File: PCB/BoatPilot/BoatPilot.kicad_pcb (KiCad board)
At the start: 2 copper layers, 40 x 40 mm, 87 parts, among them J101 battery, J102 switch, J103 SWD, J104 wind, J105 RC, J106 GPS, J108 failsafe, J109 SERVO1, J110 SERVO2, J111 SERVO3, J201 GPIO, J202 USB-Audio-IR, J203 Audio-UART, P101 ICT-Point, P102 ICT-Point, P103 ICT-Point, P104 ICT-Point, P105 ICT-Point, P106 ICT-Point, P107 ICT-Point, P108 ICT-Point, P109 ICT-Point, P113 ICT-Point, P119 ICT-Point, P129 ICT-Point, P130 ICT-Point, P132 ICT-Point, P133 ICT-Point, P134 ICT-Point, P135 ICT-Point, Q101 TSM3457, U101 GY-91, U102 74LVC1G97, U103 LM1117-3.3, U104 TPS565208, U105 24LC512, U106 74LVC1G97, U108 74LVC1G97, U109 STM32F103C8Tx, Y101 8MHz

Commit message: Add DMC to project
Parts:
- added Barcode**: BoatPilot, footprint:BoatPilot, B.Cu at (139.2, 106.6)
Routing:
- net +BATT: track 53.1 -> 55.0 mm
- net +5V: track 115.5 -> 117.0 mm
- net GND: vias 75 -> 69

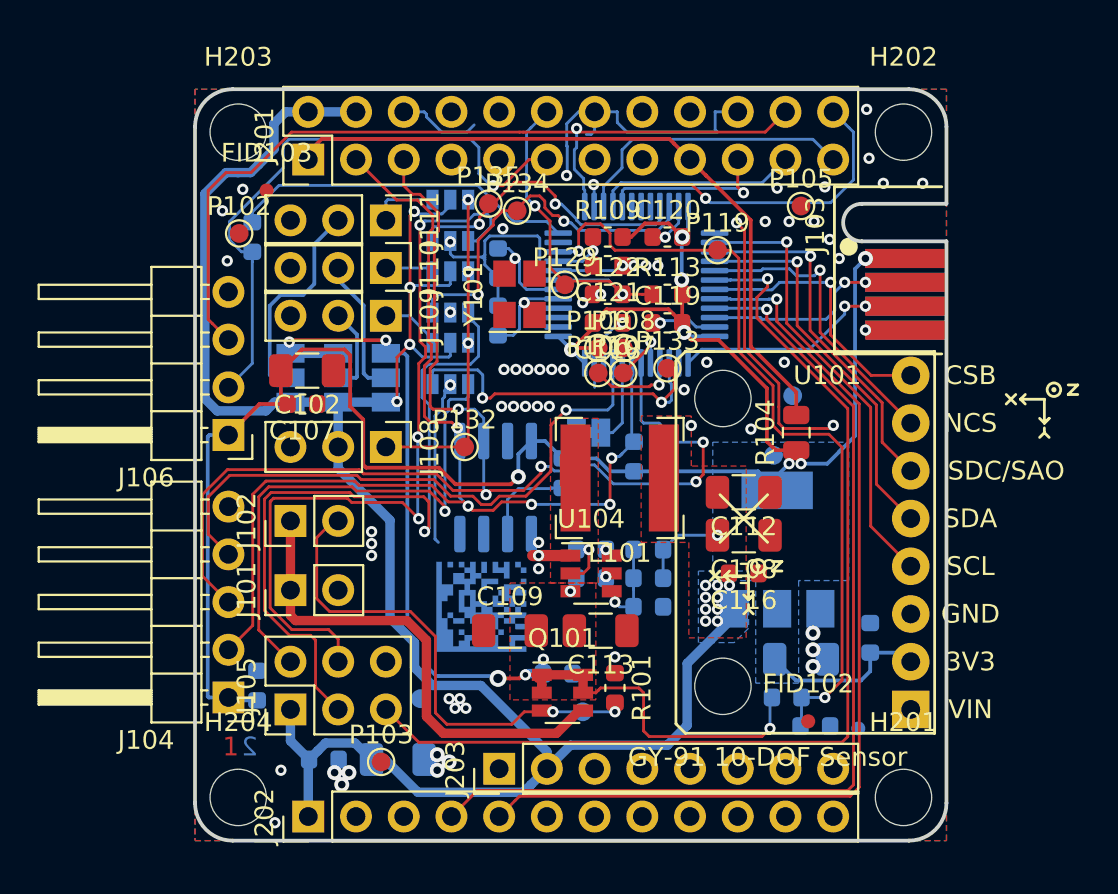
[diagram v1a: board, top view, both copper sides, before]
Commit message: Update layout
Change the LM1117 to a smaller sized LDO and adapt the layout.
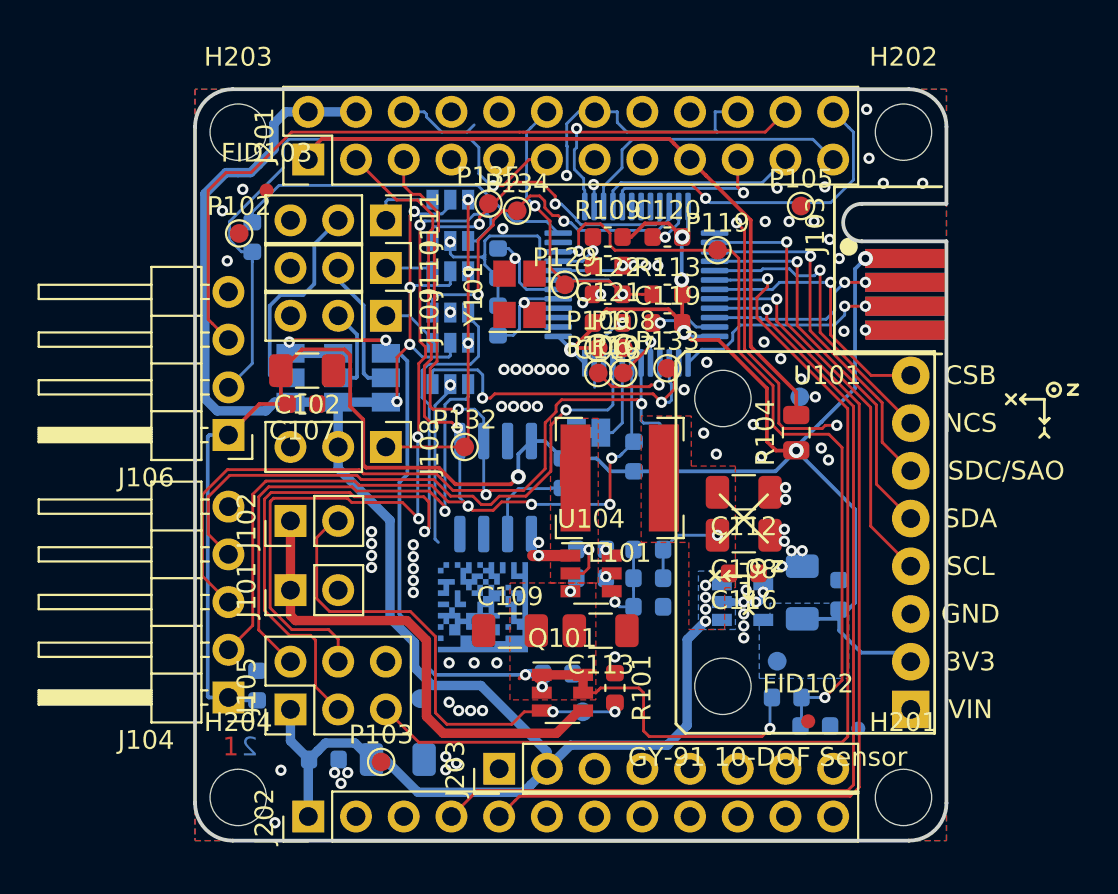
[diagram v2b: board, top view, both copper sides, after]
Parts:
- U103: value LM1117-3.3 -> TLV75733PDBV; footprint Package_TO_SOT_SMD:SOT-223-3_TabPin2 -> Package_TO_SOT_SMD:SOT-23-5
- moved P130 11.0 mm to (155.0, 109.4)
- moved C111 3.56 mm to (156.3, 105.8), turned to 270 degrees
- moved U103 3.35 mm to (153.1, 106.3), turned to 0 degrees
- moved C103 2.82 mm to (158.3, 105.9)
- moved P104 0.39 mm to (156.2, 95.4)
- moved Barcode** 0.09 mm to (139.3, 106.6), turned to 180 degrees
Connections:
- J201 pad 10: /FriednlyARM NanoPi Air/RX1 -> (no net)
- J201 pad 13: /FriednlyARM NanoPi Air/RTS2_PA2 -> (no net)
- J201 pad 15: /FriednlyARM NanoPi Air/CTS2_PA3 -> (no net)
- J201 pad 16: /FriednlyARM NanoPi Air/RTS1 -> (no net)
- J201 pad 18: /FriednlyARM NanoPi Air/CTS1 -> (no net)
- J201 pad 7: /FriednlyARM NanoPi Air/PG11 -> (no net)
- J201 pad 8: /FriednlyARM NanoPi Air/TX1 -> (no net)
- J202 pad 10: /FriednlyARM NanoPi Air/I2S_DOUT -> (no net)
- J202 pad 11: /FriednlyARM NanoPi Air/I2S_DIN -> (no net)
- J202 pad 2: /FriednlyARM NanoPi Air/D1P -> (no net)
- J202 pad 3: /FriednlyARM NanoPi Air/D1N -> (no net)
- J202 pad 6: /FriednlyARM NanoPi Air/PL11_IR -> (no net)
- J202 pad 7: /FriednlyARM NanoPi Air/PA17_SPDIF -> (no net)
- J202 pad 8: /FriednlyARM NanoPi Air/I2S_LRCK -> (no net)
- J202 pad 9: /FriednlyARM NanoPi Air/I2S_BCK -> (no net)
- J203 pad 3: /FriednlyARM NanoPi Air/TX0 -> (no net)
- J203 pad 4: /FriednlyARM NanoPi Air/RX0 -> (no net)
- J203 pad 5: /FriednlyARM NanoPi Air/LL -> (no net)
- J203 pad 6: /FriednlyARM NanoPi Air/LR -> (no net)
- J203 pad 7: /FriednlyARM NanoPi Air/MN -> (no net)
- J203 pad 8: /FriednlyARM NanoPi Air/MP -> (no net)
- U101 pad 1: Net-(U101-Pad1) -> (no net)
- U103 pad 1: GND -> +5V
- U103 pad 2: +3V3 -> GND
- U109 pad 11: Net-(U109-Pad11) -> (no net)
- U109 pad 18: Net-(U109-Pad18) -> (no net)
- U109 pad 19: Net-(U109-Pad19) -> (no net)
- U109 pad 2: Net-(U109-Pad2) -> (no net)
- U109 pad 20: Net-(U109-Pad20) -> (no net)
- U109 pad 25: Net-(U109-Pad25) -> (no net)
- U109 pad 3: Net-(U109-Pad3) -> (no net)
- U109 pad 38: Net-(U109-Pad38) -> (no net)
- U109 pad 4: Net-(U109-Pad4) -> (no net)
- U109 pad 46: Net-(U109-Pad46) -> (no net)
- Y101 pad 2: Net-(Y101-Pad2) -> (no net)
- Y101 pad 4: Net-(Y101-Pad4) -> (no net)
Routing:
- net +3V3: track 121.4 -> 128.1 mm, vias 8 -> 7
- net /I2C1_SCL: track 66.5 -> 61.5 mm, vias 5 -> 3
- net GND: track 79.6 -> 81.1 mm, vias 69 -> 95
- net +5V: track 117.0 -> 116.4 mm, vias 14 -> 9
- net +BATT: track 55.0 -> 55.2 mm, vias 7 -> 6

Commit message: Add USB pull-up resistor and connector
Add the missing pull-up resistors to the USB line and add a mini-usb
header to the board
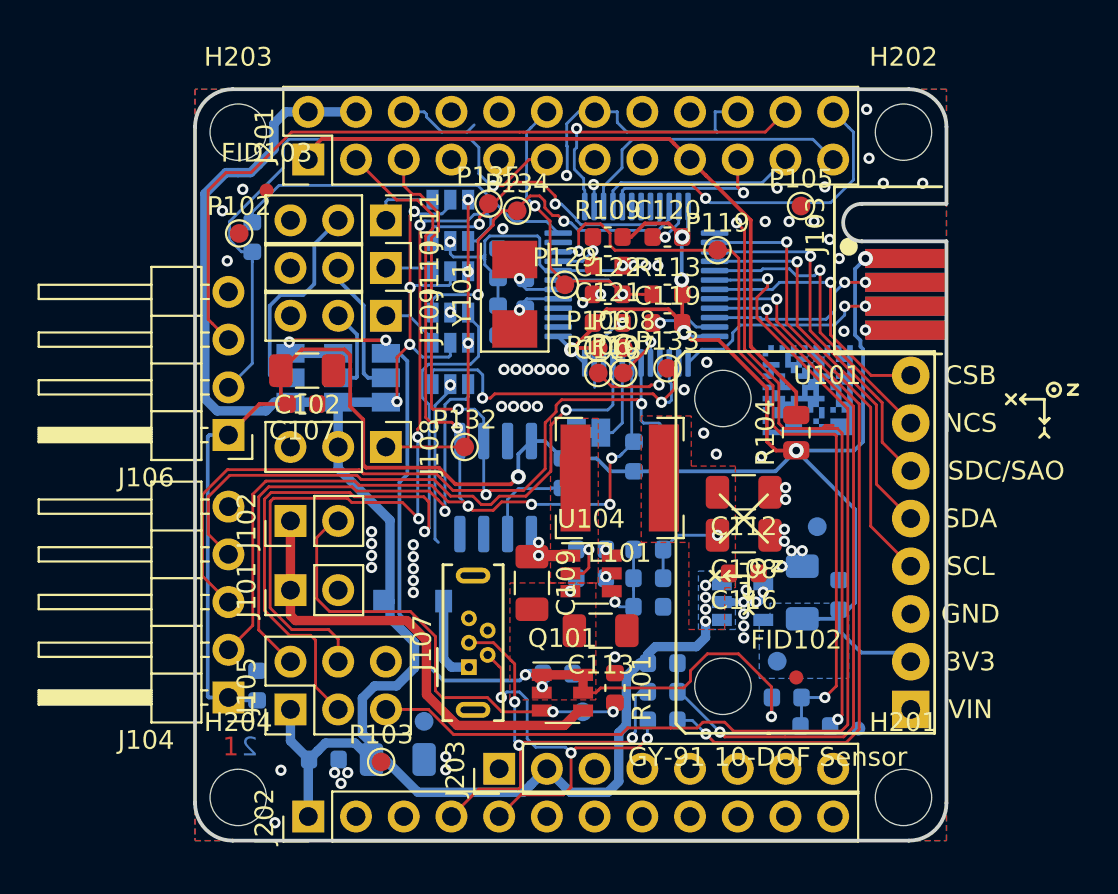
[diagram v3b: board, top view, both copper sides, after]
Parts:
- added D101: 1N4417, Diode_SMD:D_SOD-123, B.Cu at (135.6, 106.2)
- added J107: USB_OTG, Connector_USB:USB_Micro-B_Wuerth_614105150721_Vertical, F.Cu at (138.6, 109.8)
- added R107: 20R, Resistor_SMD:R_0603_1608Metric, B.Cu at (148.9, 111.1)
- added R108: 20R, Resistor_SMD:R_0603_1608Metric, B.Cu at (148.9, 112.6)
- added R112: 4.64k, Resistor_SMD:R_0603_1608Metric, B.Cu at (148.9, 109.6)
- added R116: 1M, Resistor_SMD:R_0603_1608Metric, B.Cu at (141.6, 89.9)
- Y101: footprint Crystal:Crystal_SMD_SeikoEpson_FA238-4Pin_3.2x2.5mm -> Crystal:Crystal_SMD_5032-2Pin_5.0x3.2mm
- moved Barcode** 20.8 mm to (156.6, 95.0)
- moved P104 6.97 mm to (157.1, 102.3)
- moved C109 2.80 mm to (141.9, 105.3), turned to 270 degrees
- moved FID102 2.42 mm to (156.0, 110.3)
- moved P101 1.22 mm to (136.2, 112.7)
- moved Y101 0.25 mm to (141.0, 89.9)
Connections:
- J201 pad 10: (no net) -> /FriednlyARM NanoPi Air/RX1
- J201 pad 13: (no net) -> /FriednlyARM NanoPi Air/RTS2_PA2
- J201 pad 15: (no net) -> /FriednlyARM NanoPi Air/CTS2_PA3
- J201 pad 16: (no net) -> /FriednlyARM NanoPi Air/RTS1
- J201 pad 18: (no net) -> /FriednlyARM NanoPi Air/CTS1
- J201 pad 7: (no net) -> /FriednlyARM NanoPi Air/PG11
- J201 pad 8: (no net) -> /FriednlyARM NanoPi Air/TX1
- J202 pad 10: (no net) -> /FriednlyARM NanoPi Air/I2S_DOUT
- J202 pad 11: (no net) -> /FriednlyARM NanoPi Air/I2S_DIN
- J202 pad 2: (no net) -> /FriednlyARM NanoPi Air/D1P
- J202 pad 3: (no net) -> /FriednlyARM NanoPi Air/D1N
- J202 pad 6: (no net) -> /FriednlyARM NanoPi Air/PL11_IR
- J202 pad 7: (no net) -> /FriednlyARM NanoPi Air/PA17_SPDIF
- J202 pad 8: (no net) -> /FriednlyARM NanoPi Air/I2S_LRCK
- J202 pad 9: (no net) -> /FriednlyARM NanoPi Air/I2S_BCK
- J203 pad 3: (no net) -> /FriednlyARM NanoPi Air/TX0
- J203 pad 4: (no net) -> /FriednlyARM NanoPi Air/RX0
- J203 pad 5: (no net) -> /FriednlyARM NanoPi Air/LL
- J203 pad 6: (no net) -> /FriednlyARM NanoPi Air/LR
- J203 pad 7: (no net) -> /FriednlyARM NanoPi Air/MN
- J203 pad 8: (no net) -> /FriednlyARM NanoPi Air/MP
- U101 pad 1: (no net) -> Net-(U101-Pad1)
- U109 pad 11: (no net) -> Net-(U109-Pad11)
- U109 pad 18: (no net) -> Net-(U109-Pad18)
- U109 pad 19: (no net) -> Net-(U109-Pad19)
- U109 pad 2: (no net) -> Net-(U109-Pad2)
- U109 pad 20: (no net) -> Net-(U109-Pad20)
- U109 pad 25: (no net) -> Net-(U109-Pad25)
- U109 pad 3: (no net) -> Net-(U109-Pad3)
- U109 pad 32: /USBD- -> /PA11
- U109 pad 33: /USBD+ -> /PA12
- U109 pad 38: (no net) -> Net-(U109-Pad38)
- U109 pad 4: (no net) -> Net-(U109-Pad4)
- U109 pad 46: (no net) -> Net-(U109-Pad46)
- Y101 pad 2: (no net) -> Net-(C124-Pad2)
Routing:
- net /PA12: track 0.00 -> 39.2 mm, vias 0 -> 2
- net /PA11: track 0.00 -> 38.5 mm, vias 0 -> 2
- net /USBD-: track 50.9 -> 20.6 mm, vias 1 -> 3
- net /USBD+: track 52.1 -> 23.2 mm, vias 1 -> 3
- net GND: track 81.1 -> 97.6 mm, vias 95 -> 80
- net Net-(D101-Pad2): track 0.00 -> 4.61 mm
- net +3V3: track 128.1 -> 130.5 mm
- net Net-(J102-Pad2): track 26.7 -> 25.4 mm
- net Net-(J101-Pad1): track 26.3 -> 25.3 mm
- net Net-(C124-Pad2): track 5.86 -> 6.87 mm

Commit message: Fix DRC errors and optimise USB lines
Fix the DRC errors and remove the strip lines from the USB data lines.
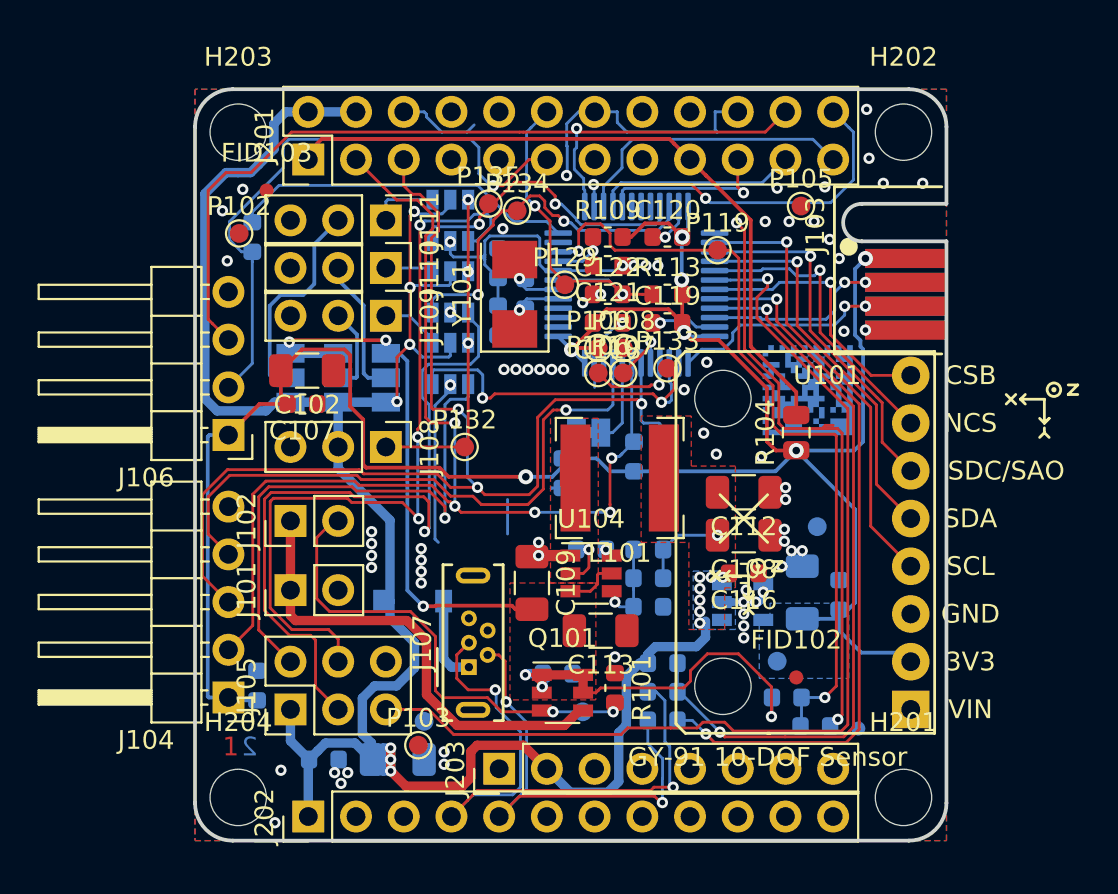
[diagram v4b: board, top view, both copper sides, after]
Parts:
- removed R106: 10k, Resistor_SMD:R_0603_1608Metric
- removed U105: 24LC512, Package_SO:SOIC-8_3.9x4.9mm_P1.27mm
- moved P103 2.17 mm to (135.9, 113.9)
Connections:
- J107 pad 4: Net-(J107-Pad4) -> (no net)
- J201 pad 10: /FriednlyARM NanoPi Air/RX1 -> (no net)
- J201 pad 13: /FriednlyARM NanoPi Air/RTS2_PA2 -> (no net)
- J201 pad 15: /FriednlyARM NanoPi Air/CTS2_PA3 -> (no net)
- J201 pad 16: /FriednlyARM NanoPi Air/RTS1 -> (no net)
- J201 pad 18: /FriednlyARM NanoPi Air/CTS1 -> (no net)
- J201 pad 7: /FriednlyARM NanoPi Air/PG11 -> (no net)
- J201 pad 8: /FriednlyARM NanoPi Air/TX1 -> (no net)
- J202 pad 10: /FriednlyARM NanoPi Air/I2S_DOUT -> (no net)
- J202 pad 11: /FriednlyARM NanoPi Air/I2S_DIN -> (no net)
- J202 pad 2: /FriednlyARM NanoPi Air/D1P -> (no net)
- J202 pad 3: /FriednlyARM NanoPi Air/D1N -> (no net)
- J202 pad 6: /FriednlyARM NanoPi Air/PL11_IR -> (no net)
- J202 pad 7: /FriednlyARM NanoPi Air/PA17_SPDIF -> (no net)
- J202 pad 8: /FriednlyARM NanoPi Air/I2S_LRCK -> (no net)
- J202 pad 9: /FriednlyARM NanoPi Air/I2S_BCK -> (no net)
- J203 pad 3: /FriednlyARM NanoPi Air/TX0 -> (no net)
- J203 pad 4: /FriednlyARM NanoPi Air/RX0 -> (no net)
- J203 pad 5: /FriednlyARM NanoPi Air/LL -> (no net)
- J203 pad 6: /FriednlyARM NanoPi Air/LR -> (no net)
- J203 pad 7: /FriednlyARM NanoPi Air/MN -> (no net)
- J203 pad 8: /FriednlyARM NanoPi Air/MP -> (no net)
- U101 pad 1: Net-(U101-Pad1) -> (no net)
- U104 pad 5: Net-(R106-Pad1) -> +BATT
- U109 pad 11: Net-(U109-Pad11) -> (no net)
- U109 pad 18: Net-(U109-Pad18) -> (no net)
- U109 pad 19: Net-(U109-Pad19) -> (no net)
- U109 pad 2: Net-(U109-Pad2) -> (no net)
- U109 pad 20: Net-(U109-Pad20) -> (no net)
- U109 pad 25: Net-(U109-Pad25) -> (no net)
- U109 pad 3: Net-(U109-Pad3) -> (no net)
- U109 pad 38: Net-(U109-Pad38) -> (no net)
- U109 pad 4: Net-(U109-Pad4) -> (no net)
- U109 pad 46: Net-(U109-Pad46) -> (no net)
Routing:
- net /USBD+: track 23.2 -> 34.0 mm, vias 3 -> 2
- net +5V: track 116.2 -> 124.7 mm, vias 9 -> 15
- net /USBD-: track 20.6 -> 24.4 mm, vias 3 -> 2
- net GND: track 97.6 -> 95.1 mm, vias 80 -> 75
- net +3V3: track 130.5 -> 128.9 mm
- net +BATT: track 55.6 -> 54.4 mm
- net /I2C1_SDA: track 59.2 -> 60.0 mm
- net /WIND_PWM: track 32.0 -> 32.8 mm
- net /RC_SERVO2: track 28.1 -> 28.8 mm
- net /I2C1_SCL: track 61.3 -> 60.7 mm
- net Net-(R106-Pad1): track 0.38 -> 0.00 mm, vias 1 -> 0

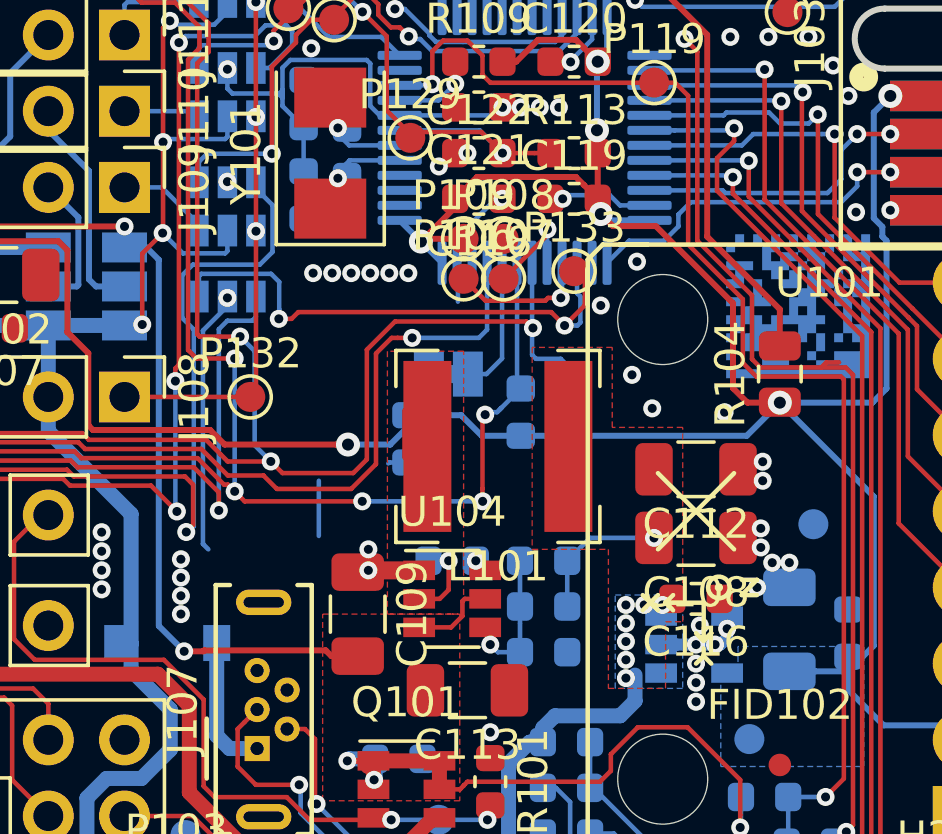
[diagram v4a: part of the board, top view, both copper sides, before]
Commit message: Readd eeporm chip
The eeprom was deleted and the SOIC was added to the layout again
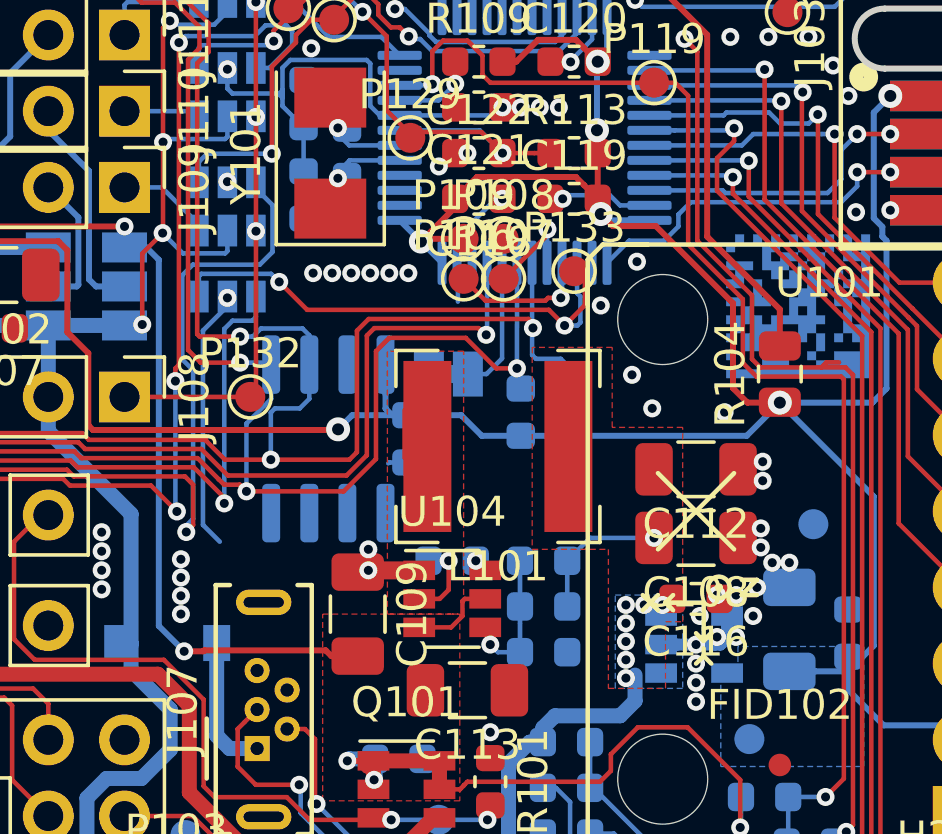
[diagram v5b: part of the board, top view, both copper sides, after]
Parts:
- added U105: 24LC512, Package_SO:SOIC-8_3.9x4.9mm_P1.27mm, B.Cu at (141.0, 99.4)
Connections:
- J107 pad 4: (no net) -> Net-(J107-Pad4)
- J201 pad 10: (no net) -> /FriednlyARM NanoPi Air/RX1
- J201 pad 13: (no net) -> /FriednlyARM NanoPi Air/RTS2_PA2
- J201 pad 15: (no net) -> /FriednlyARM NanoPi Air/CTS2_PA3
- J201 pad 16: (no net) -> /FriednlyARM NanoPi Air/RTS1
- J201 pad 18: (no net) -> /FriednlyARM NanoPi Air/CTS1
- J201 pad 7: (no net) -> /FriednlyARM NanoPi Air/PG11
- J201 pad 8: (no net) -> /FriednlyARM NanoPi Air/TX1
- J202 pad 10: (no net) -> /FriednlyARM NanoPi Air/I2S_DOUT
- J202 pad 11: (no net) -> /FriednlyARM NanoPi Air/I2S_DIN
- J202 pad 2: (no net) -> /FriednlyARM NanoPi Air/D1P
- J202 pad 3: (no net) -> /FriednlyARM NanoPi Air/D1N
- J202 pad 6: (no net) -> /FriednlyARM NanoPi Air/PL11_IR
- J202 pad 7: (no net) -> /FriednlyARM NanoPi Air/PA17_SPDIF
- J202 pad 8: (no net) -> /FriednlyARM NanoPi Air/I2S_LRCK
- J202 pad 9: (no net) -> /FriednlyARM NanoPi Air/I2S_BCK
- J203 pad 3: (no net) -> /FriednlyARM NanoPi Air/TX0
- J203 pad 4: (no net) -> /FriednlyARM NanoPi Air/RX0
- J203 pad 5: (no net) -> /FriednlyARM NanoPi Air/LL
- J203 pad 6: (no net) -> /FriednlyARM NanoPi Air/LR
- J203 pad 7: (no net) -> /FriednlyARM NanoPi Air/MN
- J203 pad 8: (no net) -> /FriednlyARM NanoPi Air/MP
- U101 pad 1: (no net) -> Net-(U101-Pad1)
- U109 pad 11: (no net) -> Net-(U109-Pad11)
- U109 pad 18: (no net) -> Net-(U109-Pad18)
- U109 pad 19: (no net) -> Net-(U109-Pad19)
- U109 pad 2: (no net) -> Net-(U109-Pad2)
- U109 pad 20: (no net) -> Net-(U109-Pad20)
- U109 pad 25: (no net) -> Net-(U109-Pad25)
- U109 pad 3: (no net) -> Net-(U109-Pad3)
- U109 pad 38: (no net) -> Net-(U109-Pad38)
- U109 pad 4: (no net) -> Net-(U109-Pad4)
- U109 pad 46: (no net) -> Net-(U109-Pad46)
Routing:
- net /I2C1_SCL: track 60.7 -> 63.9 mm
- net /I2C1_SDA: track 60.0 -> 62.8 mm, vias 5 -> 3
- net GND: track 95.1 -> 93.1 mm, vias 75 -> 78
- net +3V3: track 128.9 -> 130.5 mm
- net /SERVO2: track 19.5 -> 18.5 mm
- net /RC_SERVO2: track 28.8 -> 28.2 mm
